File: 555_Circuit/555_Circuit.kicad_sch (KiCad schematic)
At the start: 1 part

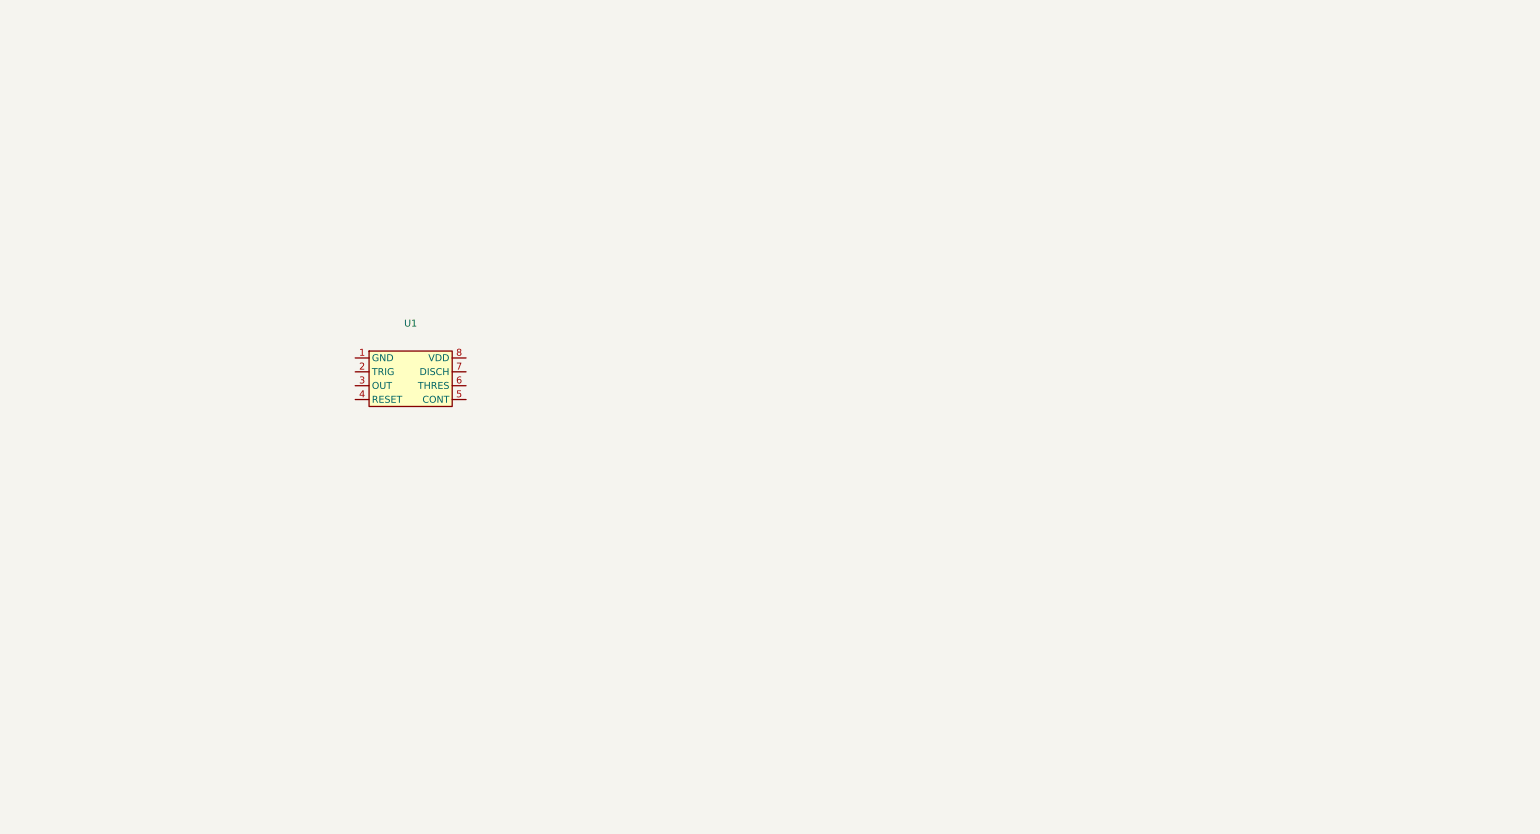
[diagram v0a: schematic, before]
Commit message: Updated 555 circuit schematic
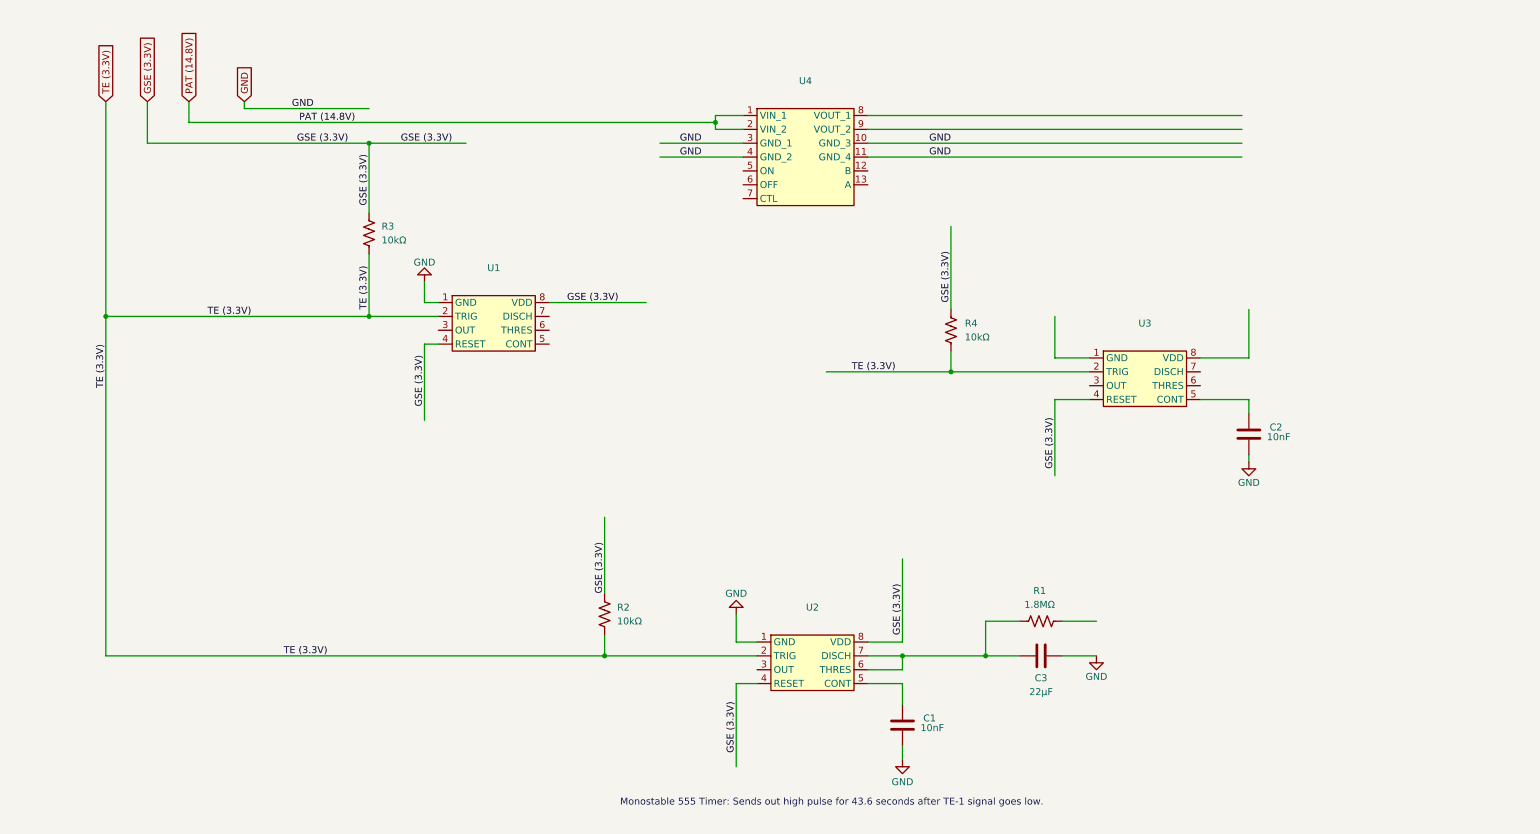
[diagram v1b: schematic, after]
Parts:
- added C1, C2: 10nF, symbol Device:C
- added C3: 22μF, symbol Device:C
- added R1: 1.8MΩ, symbol Device:R_US
- added R2, R3, R4: 10kΩ, symbol Device:R_US
- added U2, U3: ~, symbol RockSat_Sym:TLC555
- added U4: ~, symbol RockSat_Sym:Pololu_Switch
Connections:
- net GND: now reaches U1.1 (GND)
- net GND: now also C1.2, C2.2, C3.2, U2.1 (GND), U4.10 (GND_3), U4.11 (GND_4), U4.3 (GND_1), U4.4 (GND_2)
- net TE (3.3V): now reaches U1.2 (TRIG)
- net TE (3.3V): now also R2.2, R3.2, R4.2, U2.2 (TRIG), U3.2 (TRIG)
- net GSE (3.3V): now reaches U1.4 (RESET)
- net GSE (3.3V): now also U1.8 (VDD), R2.1, R3.1, R4.1, U2.4 (RESET), U2.8 (VDD), U3.4 (RESET)
- new net: C1.1, U2.5 (CONT)
- new net: C3.1, R1.1, U2.6 (THRES), U2.7 (DISCH)
- new net: C2.1, U3.5 (CONT)
- new net PAT (14.8V): U4.1 (VIN_1), U4.2 (VIN_2)
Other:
- note added: "Monostable 555 Timer: Sends out high pulse for 43.6 seconds after TE-1 signal goes low."
- moved on the sheet: U1

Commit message: Added logic inverter to the 555 timer to toggle on the battery draw to ML system
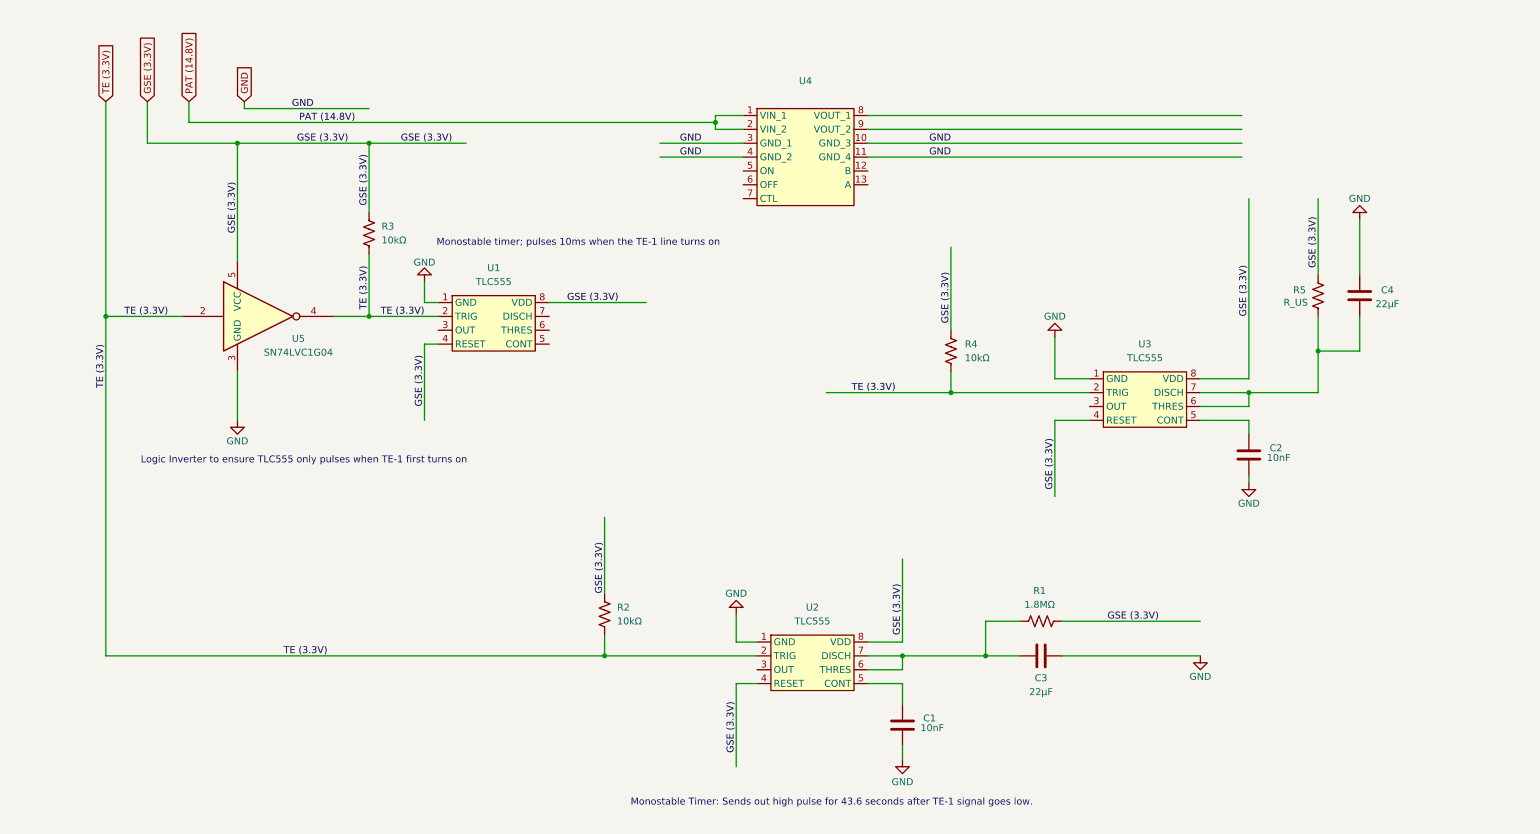
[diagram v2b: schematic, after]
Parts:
- added C4: 22μF, symbol Device:C
- added R5: R_US, symbol Device:R_US
- added U5: SN74LVC1G04, symbol 74xGxx:74LVC1G04
- U1, U2, U3: value ~ -> TLC555
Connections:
- net GND: now also U3.1 (GND), C4.2, U5.3 (GND)
- net GSE (3.3V): now also R1.2, U3.8 (VDD), R5.1, U5.5 (VCC)
- net TE (3.3V): now also U5.2, U5.4
- net at U3.6 (THRES): now also U3.7 (DISCH), C4.1, R5.2
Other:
- note added: "Logic Inverter to ensure TLC555 only pulses when TE-1 first turns on"
- note added: "Monostable Timer: Sends out high pulse for 43.6 seconds after TE-1 signal goes low."
- note added: "Monostable timer; pulses 10ms when the TE-1 line turns on"
- note removed: "Monostable 555 Timer: Sends out high pulse for 43.6 seconds after TE-1 signal goes low."
- moved on the sheet: C2, R4, U3

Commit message: Added schematic for 555 timers
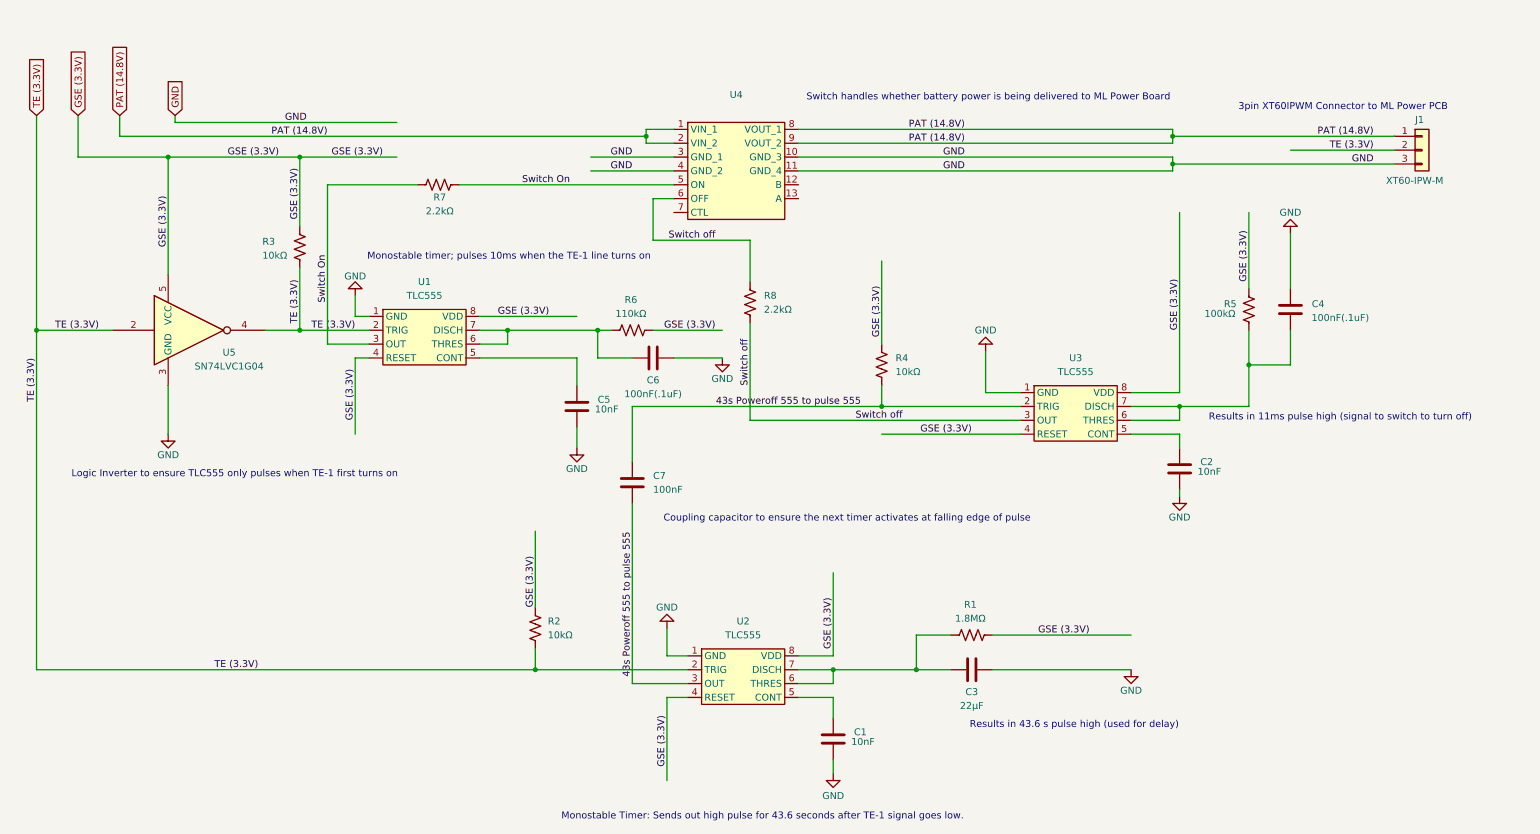
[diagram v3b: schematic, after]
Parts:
- added C5: 10nF, symbol Device:C
- added C6: 100nF(.1uF), symbol Device:C
- added C7: 100nF, symbol Device:C
- added J1: XT60-IPW-M, symbol Connector_Generic:Conn_01x03
- added R6: 110kΩ, symbol Device:R_US
- added R7, R8: 2.2kΩ, symbol Device:R_US
- C4: value 22μF -> 100nF(.1uF)
- R5: value R_US -> 100kΩ
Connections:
- net GND: now also C5.2, C6.2, J1.3 (Pin_3)
- net GSE (3.3V): now also R6.2
- net PAT (14.8V): now also U4.8 (VOUT_1), U4.9 (VOUT_2), J1.1 (Pin_1)
- net TE (3.3V): now also J1.2 (Pin_2); no longer R4.2, U3.2 (TRIG)
- net Switch On: now reaches U4.5 (ON)
- net Switch On: now also U1.3 (OUT), R7.1, R7.2
- net Switch off: now reaches U4.6 (OFF)
- net Switch off: now also U3.3 (OUT), R8.1, R8.2
- net 43s Poweroff 555 to pulse 555: now reaches U2.3 (OUT)
- net 43s Poweroff 555 to pulse 555: now also R4.2, U3.2 (TRIG), C7.1, C7.2
- net at U1.5 (CONT): now also C5.1
- net at U1.6 (THRES): now also U1.7 (DISCH), C6.1, R6.1
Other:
- note added: "3pin XT60IPWM Connector to ML Power PCB"
- note added: "Coupling capacitor to ensure the next timer activates at falling edge of pulse"
- note added: "Results in 11ms pulse high (signal to switch to turn off)"
- note added: "Results in 43.6 s pulse high (used for delay)"
- note added: "Switch handles whether battery power is being delivered to ML Power Board"
- title: (none) -> Power Distribution: ML Power Logic
- moved on the sheet: C1, C2, C3, C4, R1, R2, R3, R4, R5, U1, U2, U3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
